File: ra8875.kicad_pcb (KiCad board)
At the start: 2 copper layers, 30 x 43.2 mm, 17 parts

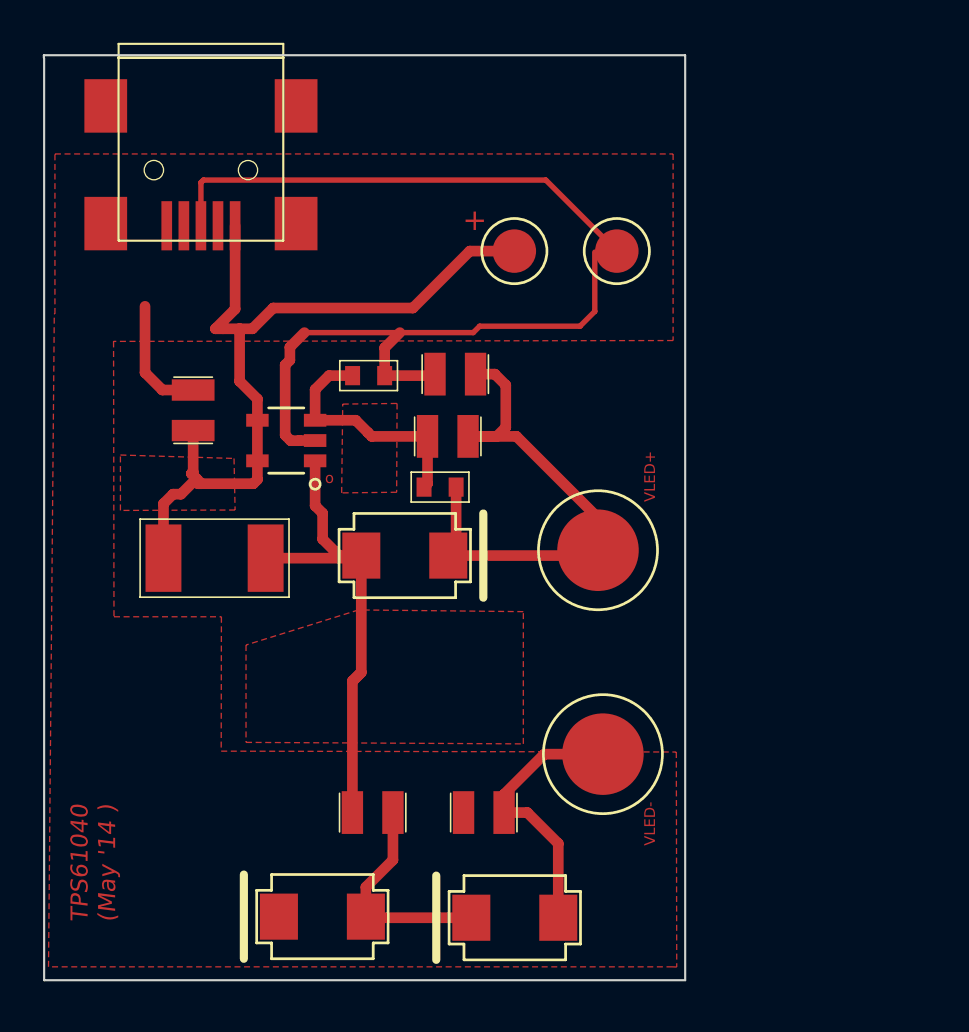
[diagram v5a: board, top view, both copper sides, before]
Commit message: Added Micrel 3.3v component
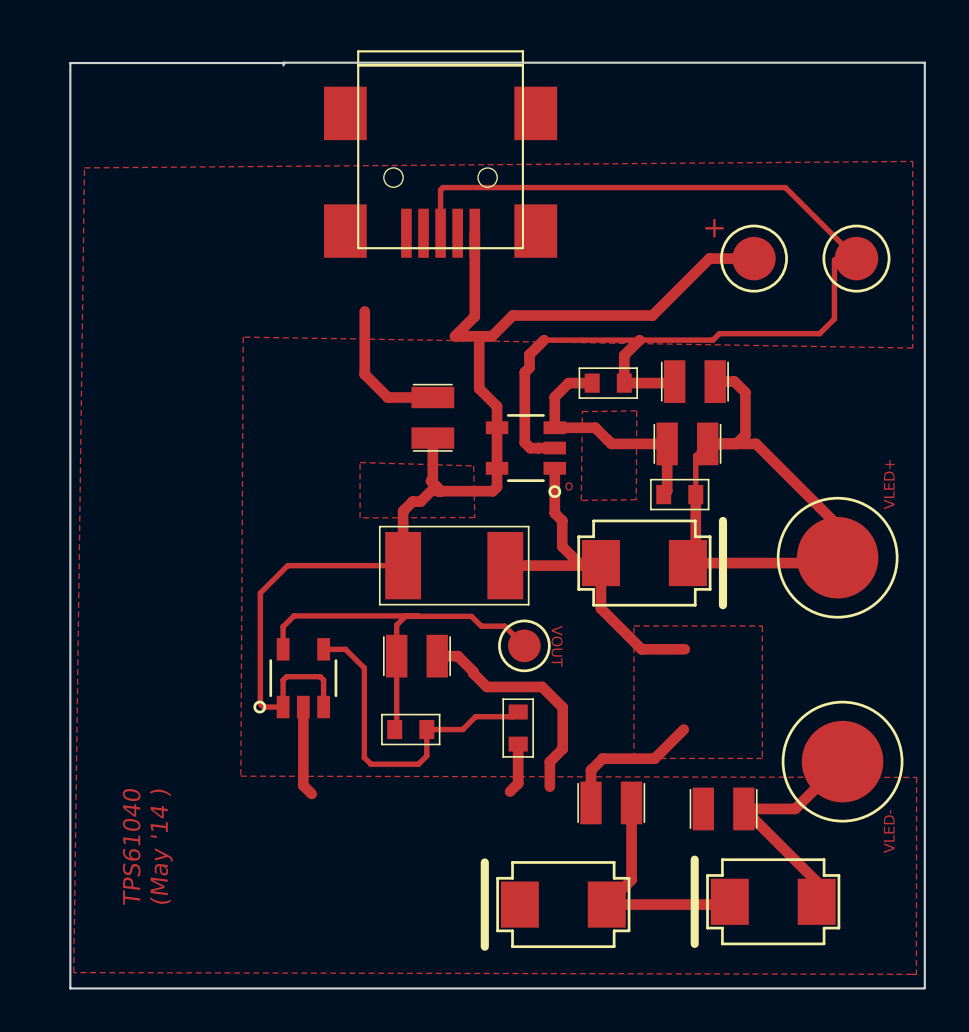
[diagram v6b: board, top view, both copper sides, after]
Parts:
- added ?: Val*, PAD_C_60x60, F.Cu at (42.8, 42.3)
- added C6: C, 0805SMDLED_BIGGER, F.Cu at (37.8, 42.7)
- added R3: R, 0603, F.Cu at (42.5, 46.1)
- added R4: R, 0603, F.Cu at (37.5, 46.2)
- added U1: MIC5225, SOT-235, F.Cu at (32.5, 43.8)
- R1: value 1.5M -> 150K
- R2: value 210K -> 10K
- moved D3 12.1 mm to (54.4, 54.2)
- moved D2 11.3 mm to (44.6, 54.4)
- moved C5 11.2 mm to (52.1, 49.9)
- moved ? 11.2 mm to (38.9, 24.1)
- moved C3 11.2 mm to (50.8, 29.9)
- moved D1 11.2 mm to (48.4, 38.4)
- moved PAD_C_150x150 11.2 mm to (57.4, 38.1)
- moved R2 11.2 mm to (46.7, 30.0)
- moved TPS1 11.2 mm to (42.9, 33.0)
- moved C1 11.2 mm to (38.5, 31.6)
- moved L1 11.2 mm to (39.5, 38.5)
- moved ? 11.2 mm to (53.5, 24.2)
- moved ? 11.2 mm to (58.3, 24.2)
- moved C2 11.2 mm to (50.4, 32.8)
- moved PAD_C_150x150 11.2 mm to (57.6, 47.7)
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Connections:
- C1 pad 1: Net-(C1-Pad1) -> 5V
- C2 pad 1: Net-(C2-Pad1) -> N-000008
- C3 pad 1: Net-(C2-Pad1) -> N-000008
- C5 pad 1: Net-(C5-Pad1) -> N-000001
- D1 pad 2: Net-(C2-Pad1) -> N-000008
- D3 pad 1: Net-(C5-Pad1) -> N-000001
- L1 pad 2: Net-(C1-Pad1) -> 5V
- R1 pad 1: Net-(C2-Pad1) -> N-000008
- TPS1 pad 4: Net-(C1-Pad1) -> /PWM
- TPS1 pad 5: Net-(C1-Pad1) -> 5V
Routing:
- net Net-(C1-Pad1): track 38.4 -> 5.97 mm
- net 5V: track 0.00 -> 29.3 mm
- net /PWM: track 0.00 -> 21.2 mm
- net N-000008: track 0.00 -> 20.5 mm
- net /VOUT: track 0.00 -> 19.2 mm
- net GND: track 56.7 -> 75.0 mm
- net Net-(C2-Pad1): track 25.2 -> 7.25 mm
- net N-000005: track 0.00 -> 15.5 mm
- net Net-(C5-Pad1): track 12.8 -> 3.13 mm
- net N-000001: track 0.00 -> 8.15 mm
- net N-000009: track 23.2 -> 23.9 mm
- net N-000002: track 10.3 -> 11.0 mm
- added copper zone on F.Cu, net Net-(C2-Pad2)
- removed copper zone on F.Cu, net N-000006
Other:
- board size 30 x 43.2 mm -> 39.9 x 43.3 mm
- board text added: "VOUT"

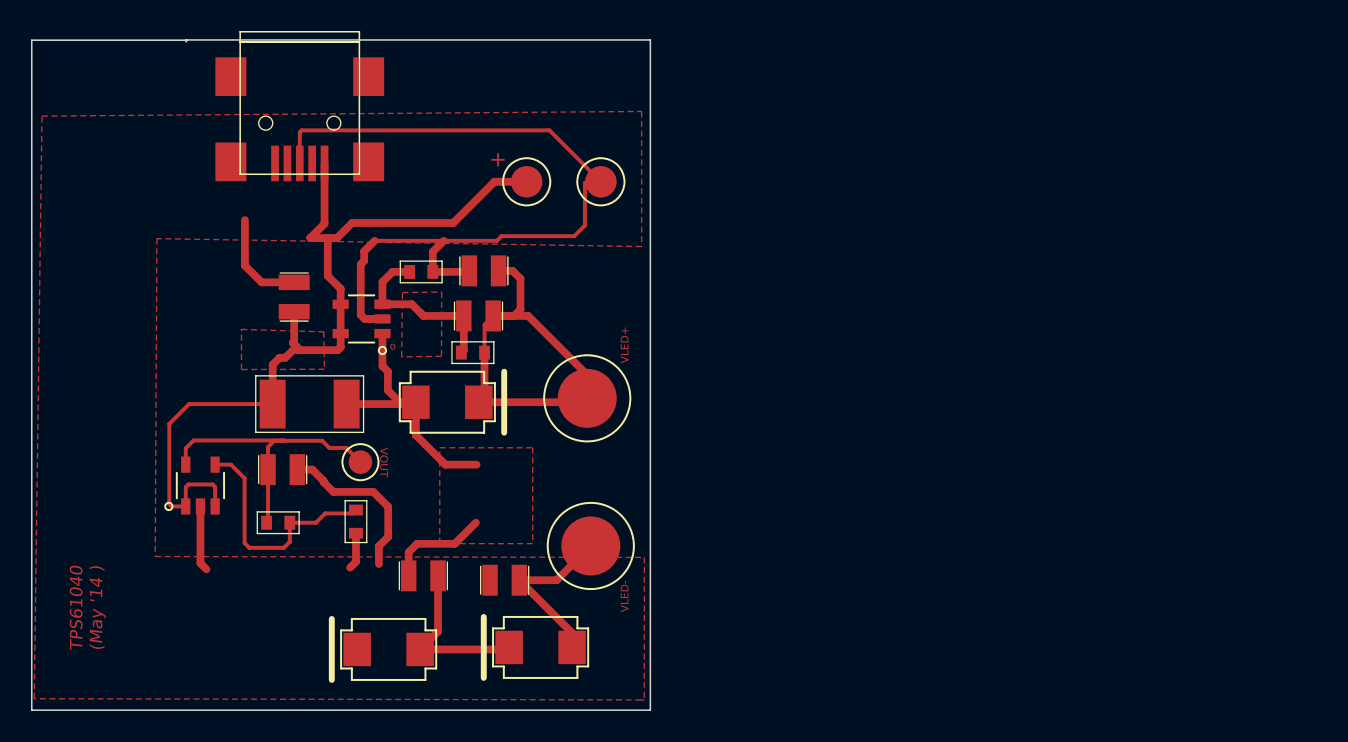
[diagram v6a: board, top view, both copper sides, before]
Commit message: Modify layout to reduce the amount of copper pour and also component placement to make it easier to solder
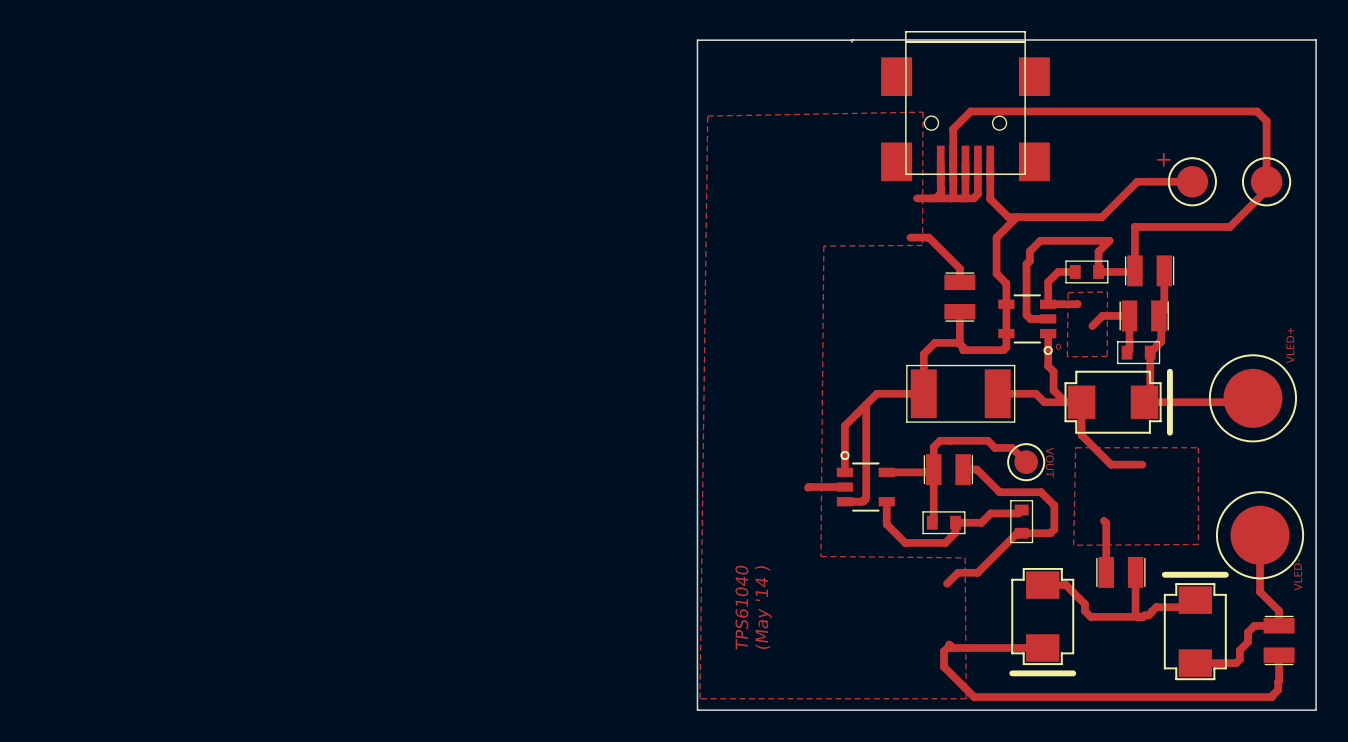
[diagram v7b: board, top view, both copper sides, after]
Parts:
- moved C5 50.1 mm to (102.1, 53.8), turned to 270 degrees
- moved C4 45.0 mm to (91.9, 49.4)
- moved PAD_C_150x150 43.2 mm to (100.9, 47.0)
- moved ? 43.0 mm to (101.3, 24.2)
- moved ? 43.0 mm to (96.5, 24.2)
- moved C2 43.0 mm to (93.4, 32.8)
- moved C6 43.0 mm to (80.7, 42.7)
- moved R1 43.0 mm to (93.0, 35.2)
- moved R3 43.0 mm to (85.5, 46.1)
- moved TPS1 43.0 mm to (85.8, 33.0)
- moved ? 43.0 mm to (81.8, 24.1)
- moved ? 43.0 mm to (85.8, 42.3)
- moved C1 43.0 mm to (81.5, 31.6)
- moved C3 43.0 mm to (93.7, 29.9)
- moved D1 43.0 mm to (91.4, 38.4)
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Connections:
- PAD_C_150x150 pad 1: Net-(C5-Pad1) -> N-000001
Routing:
- net GND: track 75.0 -> 126.0 mm
- net /PWM: track 21.2 -> 8.33 mm
- net Net-(C1-Pad1): track 5.97 -> 16.8 mm
- net Net-(C2-Pad1): track 7.25 -> 0.35 mm
- net N-000001: track 8.15 -> 13.5 mm
- net N-000008: track 20.5 -> 15.9 mm
- net /VOUT: track 19.2 -> 14.7 mm
- net N-000005: track 15.5 -> 11.9 mm
- net N-000002: track 11.0 -> 14.4 mm
- net Net-(C5-Pad1): track 3.13 -> 0.00 mm
- net N-000009: track 23.9 -> 21.8 mm
- net 5V: track 29.3 -> 28.3 mm
- net N-000006: track 11.5 -> 10.5 mm
- added copper zone on F.Cu, net N-000006
- removed copper zone on F.Cu, net Net-(C1-Pad1)
- removed copper zone on F.Cu, net Net-(C2-Pad2)
